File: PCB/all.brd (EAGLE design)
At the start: 45 x 45 mm, 122 parts, among them J1 ISP Programmer, J8 BL-HP20AUW2C, U1 ATTINY1634MLF20, U2 3.3V_REG, U3 MPU-6050-1, U4 BQ51013B_RHL_20, U5 MCP73831, U6 CAT4139, U7 BQ51013B_RHL_20, U8 BQ51013B_RHL_20, U9 BQ51013B_RHL_20

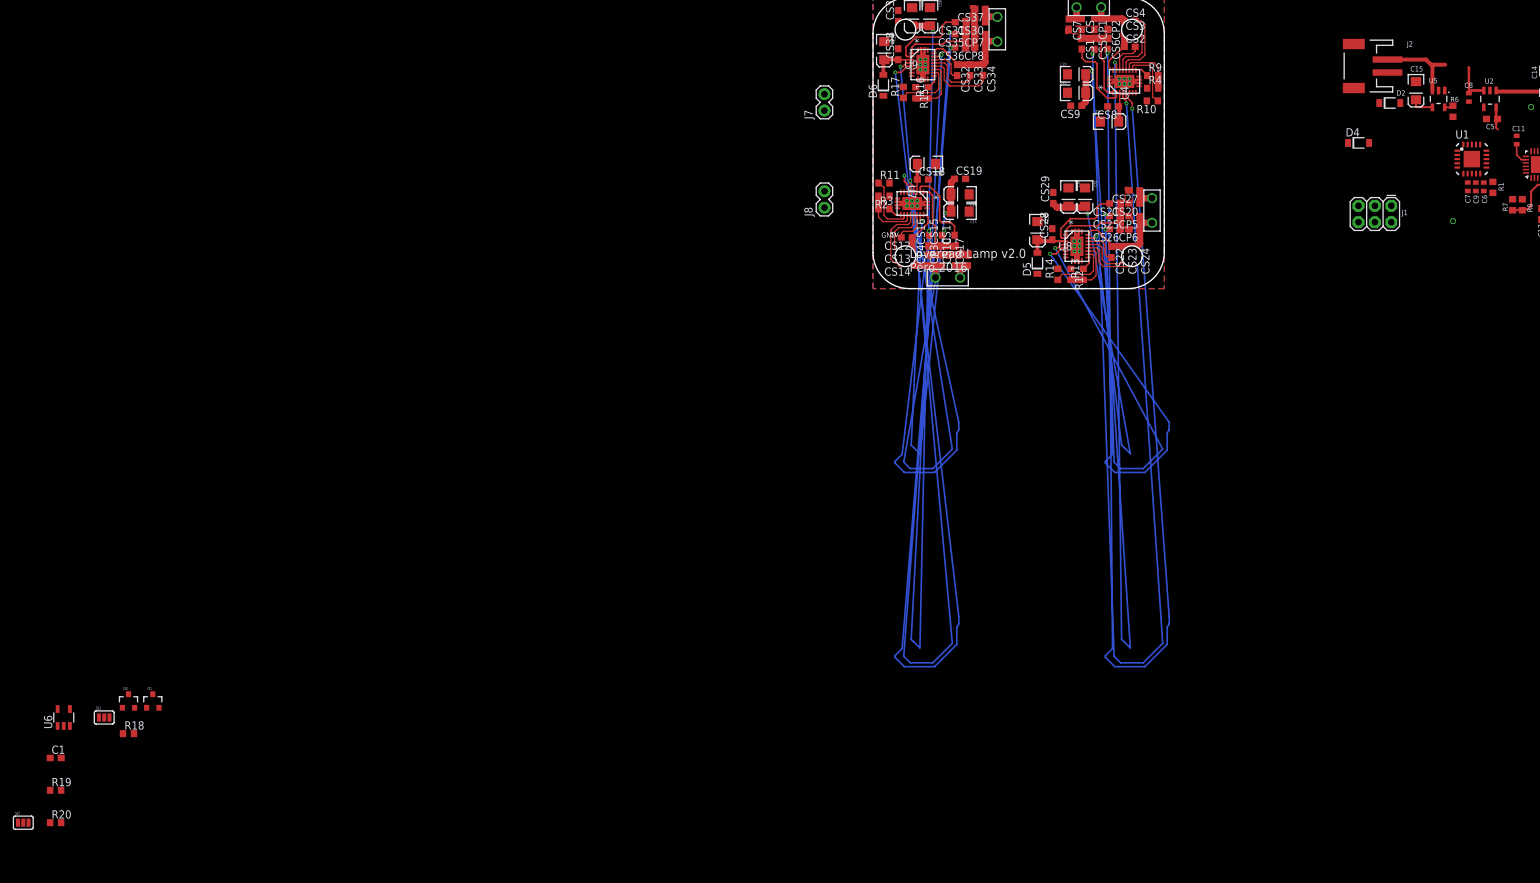
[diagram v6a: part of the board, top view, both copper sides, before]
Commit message: Adds buck converter
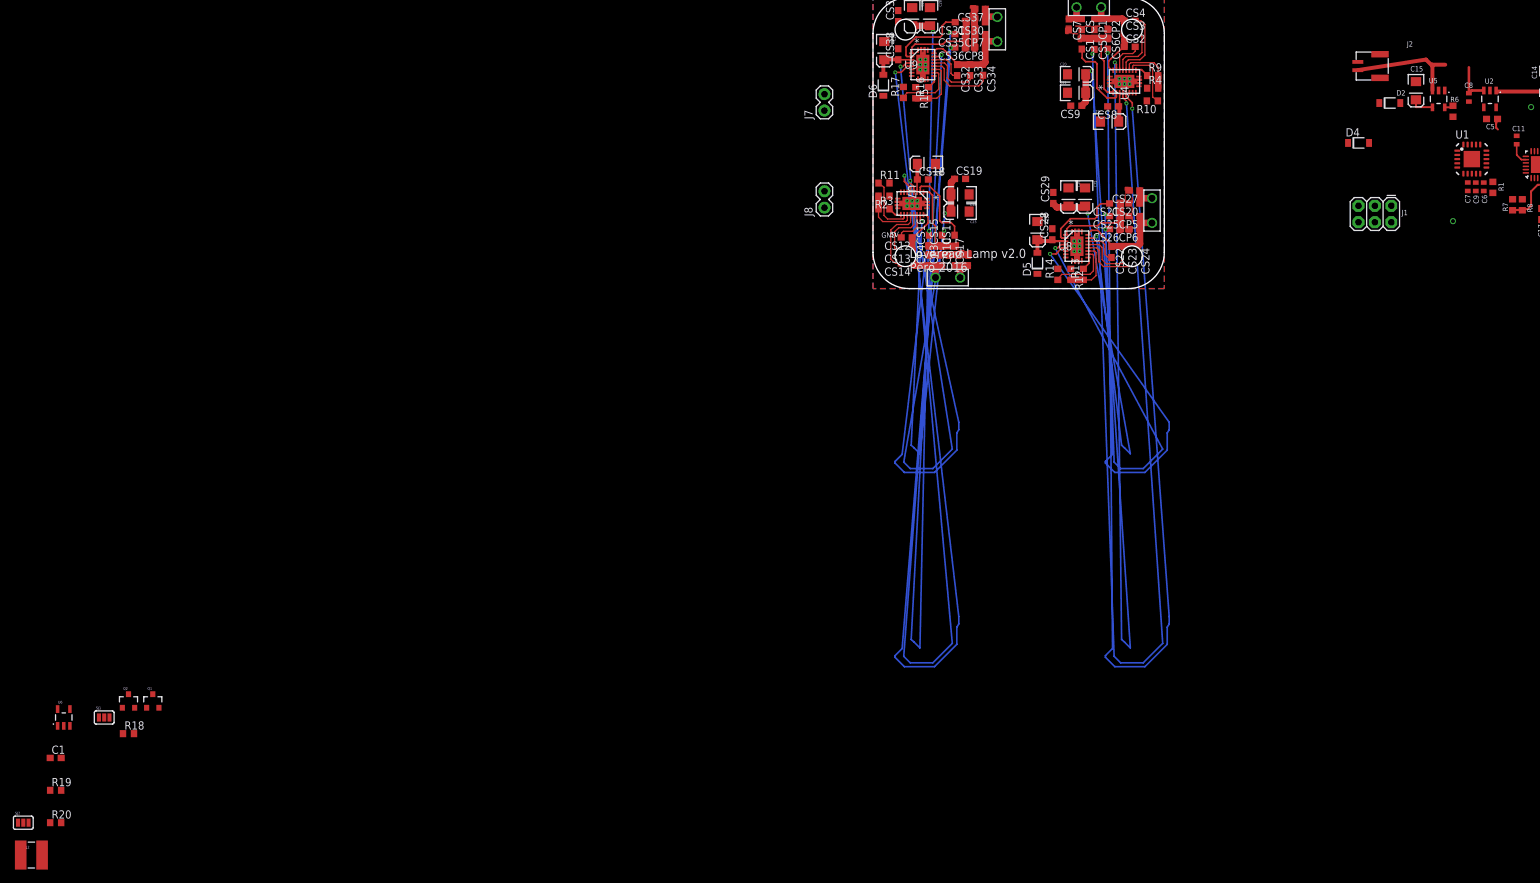
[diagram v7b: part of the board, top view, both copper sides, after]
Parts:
- added L2: 22uH, SparkFun-Passives:SDR0403
- C5: value 1μF -> 10μF
- J2: value (none) -> LIPO-BATTERY-CONNECTOR; device SparkFun-Connectors:JST-2-SMD -> pero_library:JST-LIPO-CONNECTOR-1.25MM
- U2: value 3.3V_REG -> LM3671; device SparkFun:SOT23-5 -> pero_library:SOT23-5
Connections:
- new net N$66: L2.P$1, U2.5
- net 3.3V: now also L2.P$2, U2.4; no longer U2.5
- net GND: now also J2.P$2; no longer J2.1
- net VBAT: now also J2.P$1; no longer J2.2
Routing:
- net VBAT: track 13.3 -> 18.0 mm
- net 3.3V: track 21.6 -> 19.1 mm

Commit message: rerouted Qi chargers and finished arrangements
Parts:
- removed C21, C23, C26, C29: 10μF, SparkFun:EIA3216
- C20, C22, C25, C28: device SparkFun:EIA3216 -> rcl:C0603
- moved L2 257.3 mm to (99.0, 29.6), turned to 90 degrees
- moved R20 245.1 mm to (73.6, 59.4), turned to 90 degrees
- moved SJ2 245.0 mm to (68.7, 59.1), flipped to the bottom, turned to 180 degrees
- moved R19 243.5 mm to (75.1, 59.4), turned to 270 degrees
- moved C1 238.2 mm to (72.0, 59.4), turned to 270 degrees
- moved U6 230.9 mm to (68.7, 59.4), turned to 270 degrees
- moved R18 229.2 mm to (77.0, 56.4), turned to 270 degrees
- moved SJ1 225.8 mm to (70.8, 56.5), flipped to the bottom
- moved Q2 224.4 mm to (74.5, 56.5), turned to 90 degrees
- moved Q1 217.6 mm to (70.6, 55.7), turned to 180 degrees
- moved J8 86.8 mm to (67.5, 56.2), turned to 270 degrees
- moved D2 77.2 mm to (3.73, 15.9), turned to 180 degrees
- moved L1 67.7 mm to (68.7, 63.4), turned to 180 degrees
- moved J7 64.7 mm to (57.2, 25.6), turned to 0 degrees
- moved C17 62.4 mm to (63.3, 59.4), turned to 90 degrees
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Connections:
- net GND: now also C20.2, C22.2, C25.2, C28.2; no longer C20.C, C21.C, C22.C, C23.C, C25.C, C26.C, C28.C, C29.C
- net N$23: now also C20.1; no longer C20.A, C21.A
- net N$32: now also C22.1; no longer C22.A, C23.A
- net N$45: now also C25.1; no longer C25.A, C26.A
- net N$58: now also C28.1; no longer C28.A, C29.A
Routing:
- net N$58: track 195.0 -> 2.56 mm, vias 2 -> 0
- net N$56: track 198.1 -> 11.1 mm, vias 2 -> 0
- net N$55: track 199.1 -> 13.7 mm, vias 2 -> 0
- net N$23: track 187.9 -> 2.51 mm, vias 2 -> 0
- net N$20: track 192.0 -> 13.7 mm, vias 2 -> 0
- net N$21: track 188.8 -> 11.1 mm, vias 2 -> 0
- net N$29: track 95.2 -> 14.2 mm, vias 2 -> 0
- net N$32: track 81.3 -> 2.91 mm, vias 2 -> 0
- net N$30: track 90.3 -> 12.6 mm, vias 2 -> 0
- net N$45: track 79.6 -> 2.72 mm, vias 2 -> 0
- net N$43: track 85.6 -> 11.1 mm, vias 2 -> 0
- net N$42: track 88.1 -> 13.7 mm, vias 2 -> 0
- net VBAT: track 18.0 -> 2.66 mm
- net SDA: track 0.00 -> 13.2 mm
- net N$57: track 19.6 -> 6.52 mm
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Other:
- board text removed: "+"
